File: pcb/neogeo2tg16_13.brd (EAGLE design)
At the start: 53.2 x 53.2 mm, 8 parts, among them IC5 74HC157N

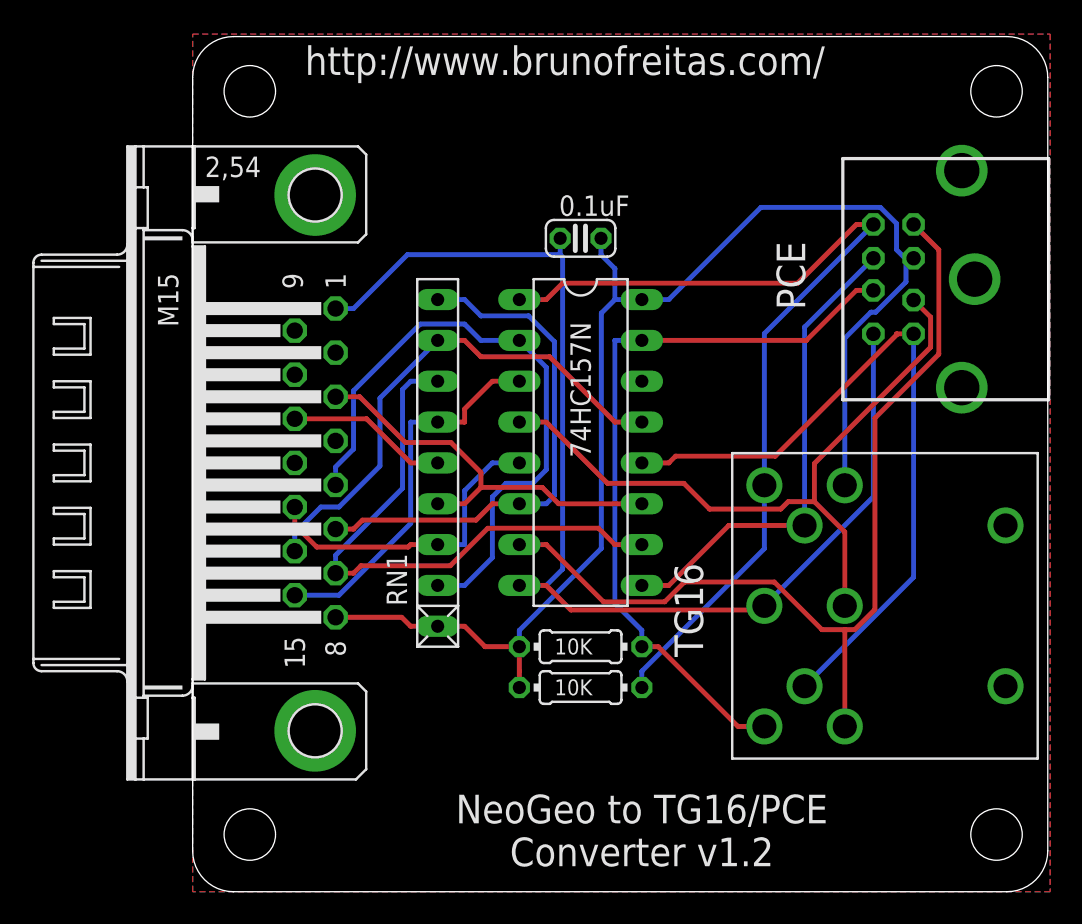
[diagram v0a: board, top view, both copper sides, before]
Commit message: Fixed start button not working in the NeoGeo to TG16 adapter
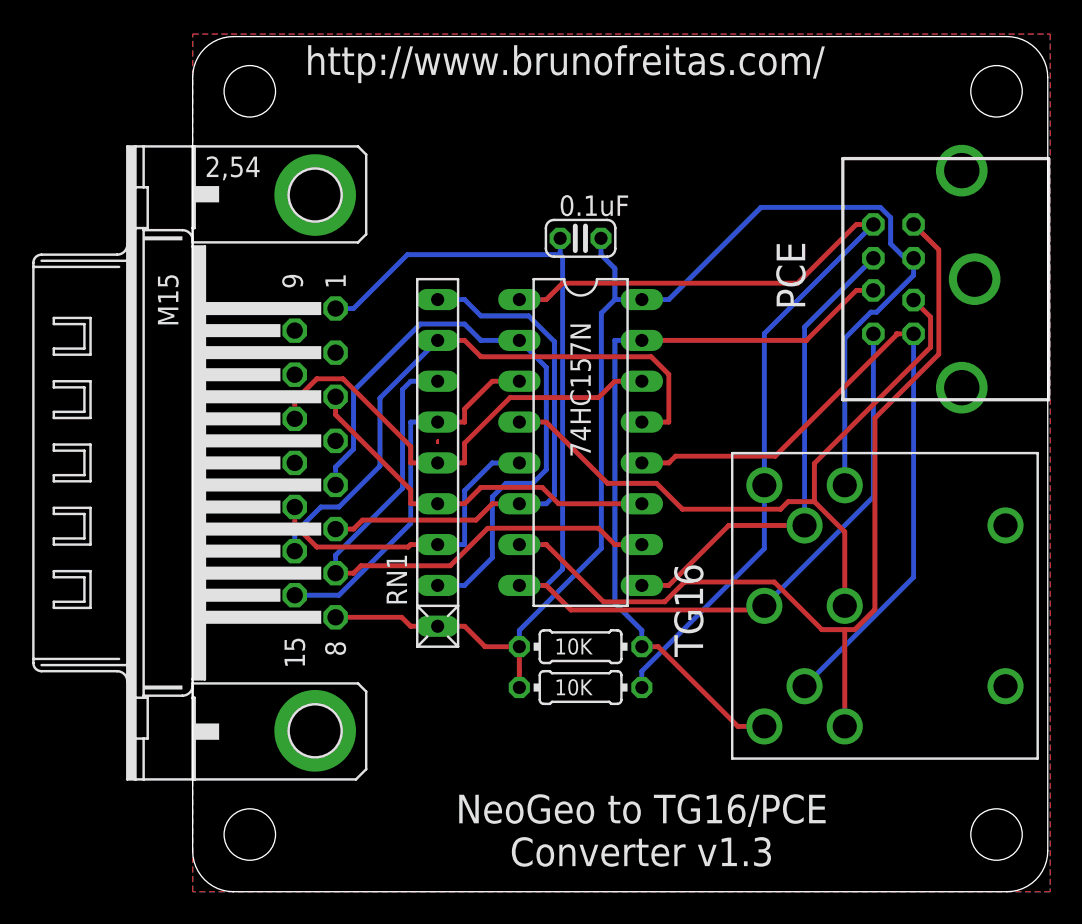
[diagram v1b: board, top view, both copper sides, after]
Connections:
- removed net RUN: IC5.14
- net START: now also IC5.14
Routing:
- net START: track 10.0 -> 28.9 mm
- net LEFT: track 32.3 -> 37.3 mm
- net GND: track 0.00 -> 4.06 mm
- net SELECT: track 25.5 -> 23.8 mm
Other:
- board text added: "NeoGeo to TG16/PCE Converter v1.3"
- board text removed: "NeoGeo to TG16/PCE Converter v1.2"
